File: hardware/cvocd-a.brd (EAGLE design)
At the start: 152.5 x 43.6 mm, 71 parts, among them IC1 PIC16F1825SO14, IC2 74HC595D, IC3 74HC595D, IC4 MCP4728_QUAD_DAC, IC5 LM324D, IC6 REG1117, IC7 6N138

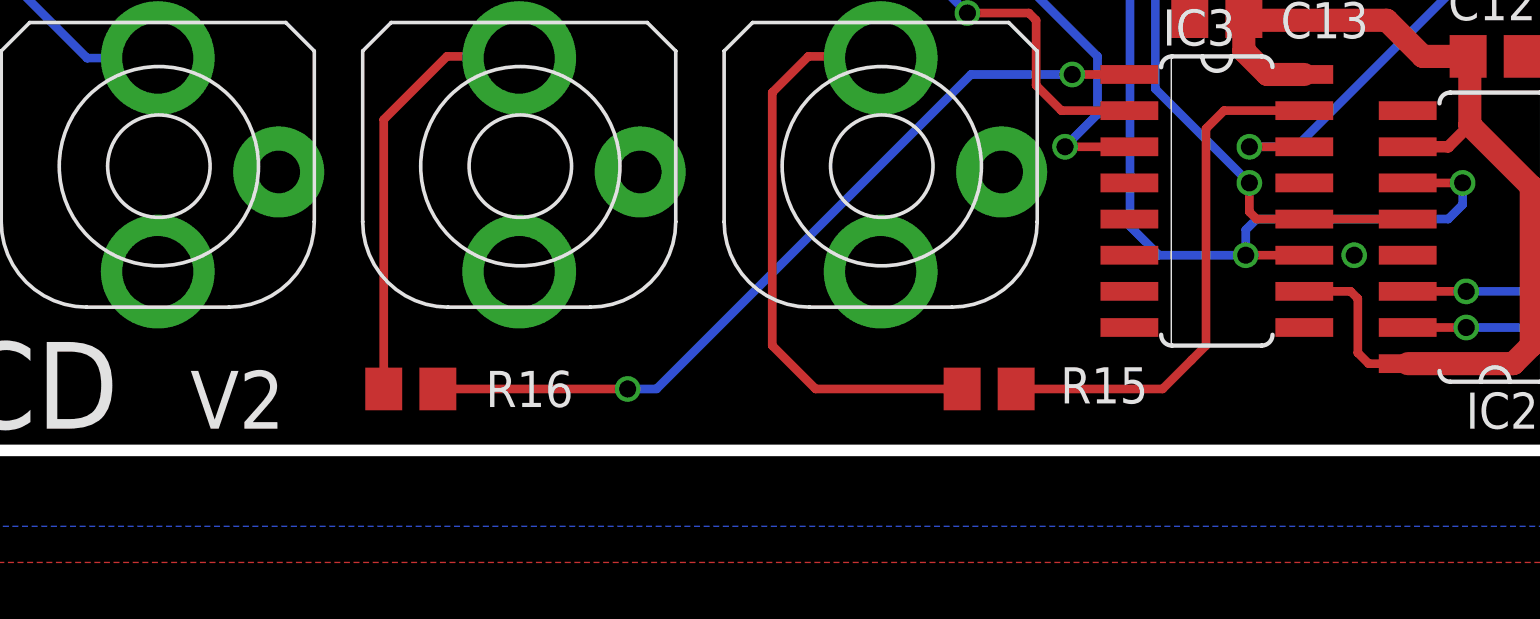
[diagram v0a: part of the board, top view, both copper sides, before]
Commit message: license logo
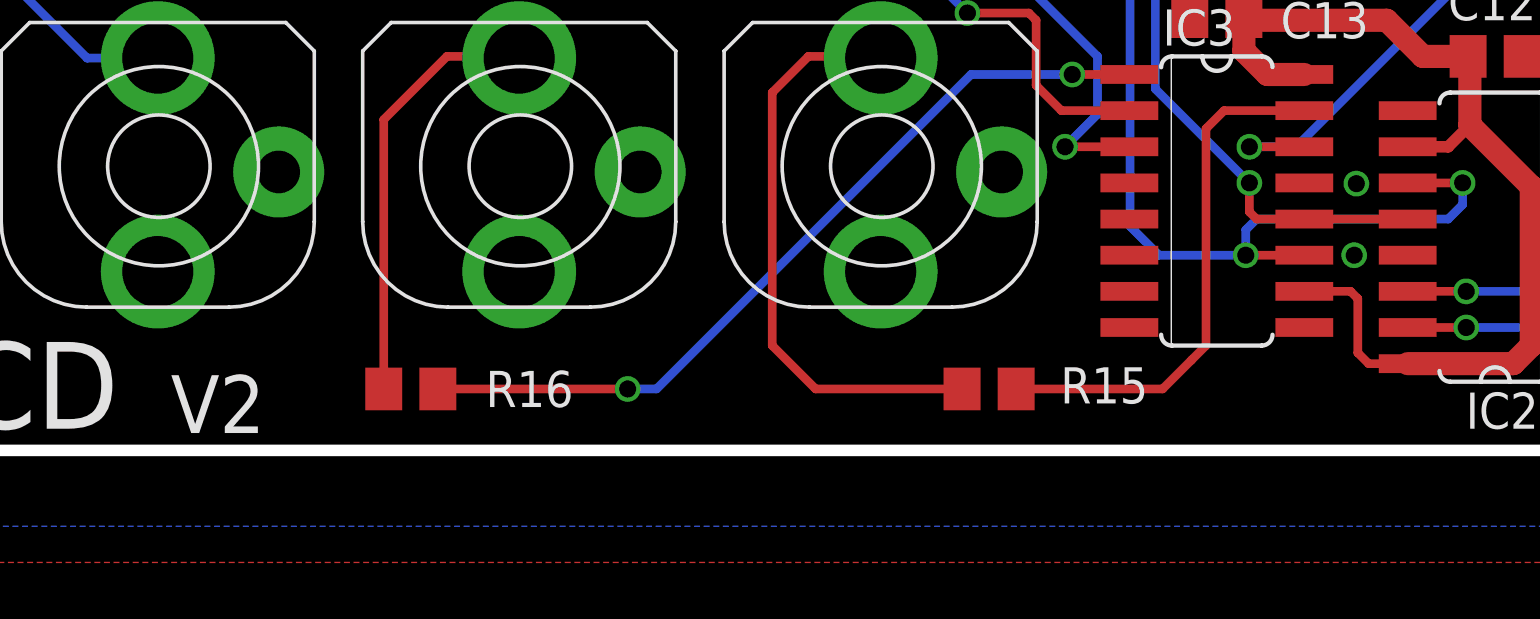
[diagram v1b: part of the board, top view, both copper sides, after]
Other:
- board text added: "six4pix.com/cvocd"
